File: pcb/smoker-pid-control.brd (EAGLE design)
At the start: 100 x 70 mm, 17 parts, among them J1 J10MM, Q1 IRLIZ44N, SW1 EC12E_SW

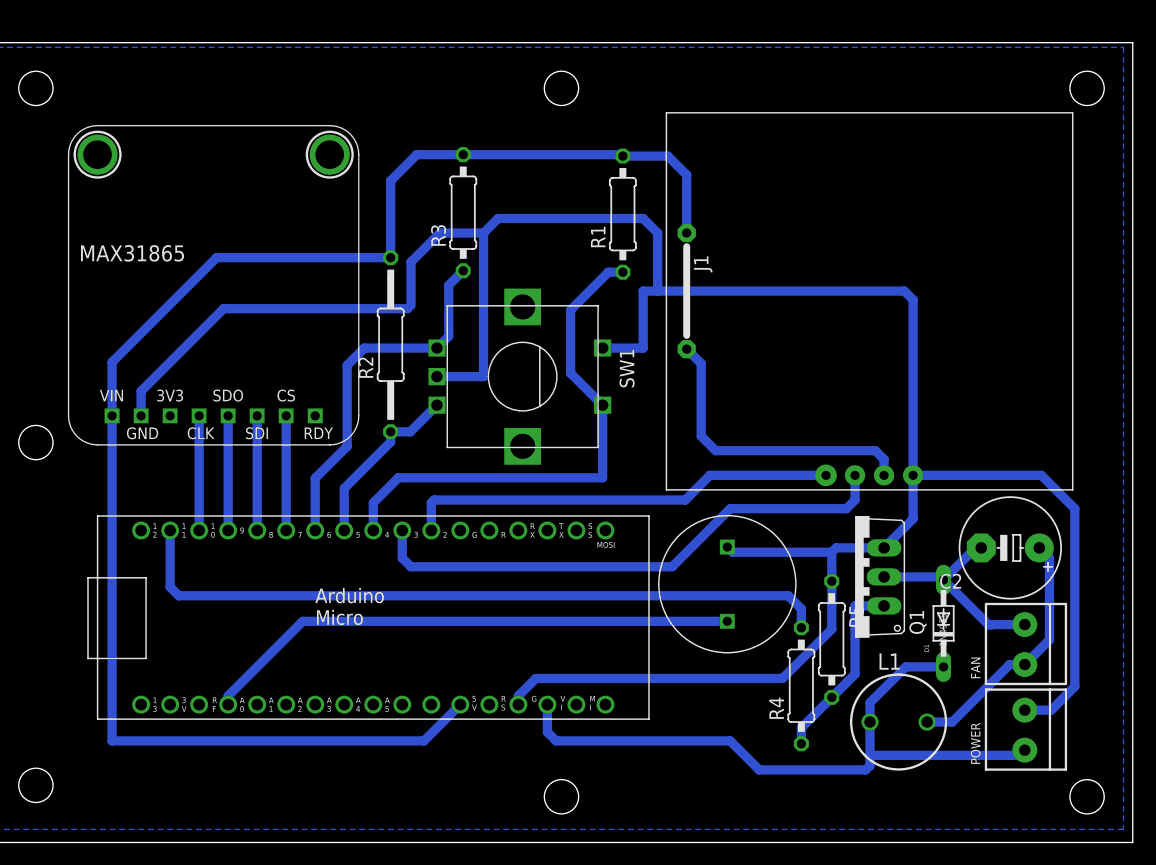
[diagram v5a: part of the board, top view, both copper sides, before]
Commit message: fix Micro power path from Vin to 5V pin, separate 5V and 12V supply
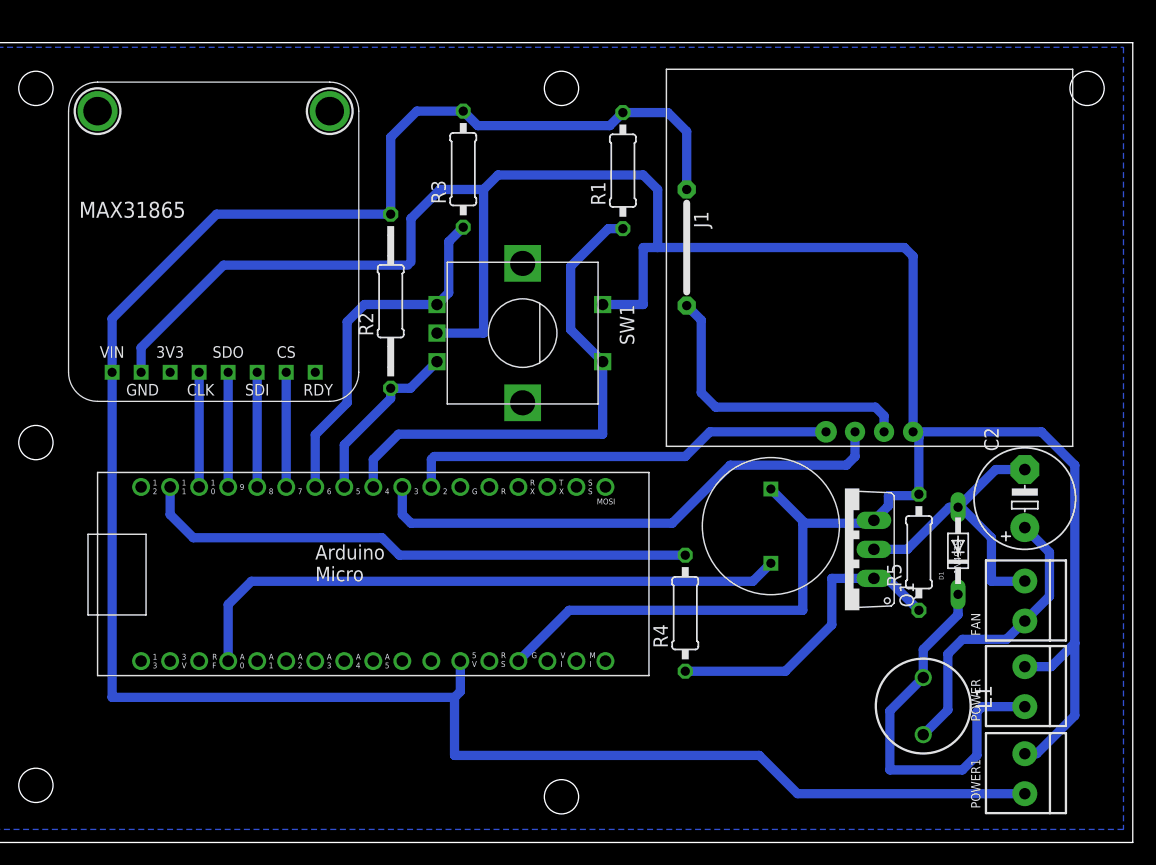
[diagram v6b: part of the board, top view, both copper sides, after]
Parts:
- added POWER1: 5V, smoker-pid-control:TERMBLOCK_1X2-3.5MM
- moved R4 12.0 mm to (60.8, 20.1)
- moved R5 10.8 mm to (81.3, 25.4), turned to 90 degrees
- moved D1 6.48 mm to (84.7, 25.5)
- moved U$3 6.35 mm to (68.3, 27.7)
- moved C2 4.50 mm to (90.6, 30.1), turned to 90 degrees
- moved FAN 3.81 mm to (90.6, 21.1)
- moved J1 3.81 mm to (61.0, 52.1)
- moved R1 3.81 mm to (55.4, 58.8)
- moved R2 3.81 mm to (35.1, 47.4)
- moved SW1 3.81 mm to (46.6, 44.6)
- moved U$1 3.81 mm to (19.6, 52.6)
- moved U$2 3.81 mm to (80.8, 35.9)
- moved PCB1 3.81 mm to (9.40, 14.6)
- moved POWER 3.81 mm to (90.6, 13.6)
- moved R3 3.81 mm to (41.4, 58.9)
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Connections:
- removed net +12V: D1.C, L1.1, PCB1.VIN, POWER.2
- new net N$15: D1.C, L1.1, POWER.2
- net +5V: now also POWER1.2
- net GND: now also POWER1.1, R5.2; no longer R5.1
- net N$12: now also R5.1; no longer R5.2
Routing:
- net +12V: track 59.1 -> 0.00 mm
- net +5V: track 132.5 -> 191.4 mm
- net N$15: track 0.00 -> 34.2 mm
- net PWM: track 62.6 -> 49.0 mm
- net N$12: track 16.6 -> 27.4 mm
- net GND: track 220.9 -> 230.2 mm
- net N$14: track 18.5 -> 26.9 mm
- net N$10: track 47.2 -> 53.9 mm
- net N$11: track 22.1 -> 25.9 mm
